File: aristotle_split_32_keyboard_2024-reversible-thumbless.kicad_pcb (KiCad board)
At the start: 2 copper layers, 100 x 87.7 mm, 41 parts, among them J1 8P8C, J2 Screw_Terminal_01x04, J3 Screw_Terminal_01x04, K13 SW_SPDT, K14 SW_SPDT, K15 SW_SPDT, K16 SW_SPDT, K17 SW_SPDT, K23 SW_SPDT, K24 SW_SPDT, K25 SW_SPDT, K26 SW_SPDT, K27 SW_SPDT, K4 SW_SPDT, K5 SW_SPDT, K6 SW_SPDT, K7 SW_SPDT, SW1 SW_SPDT, U1 ProMicro

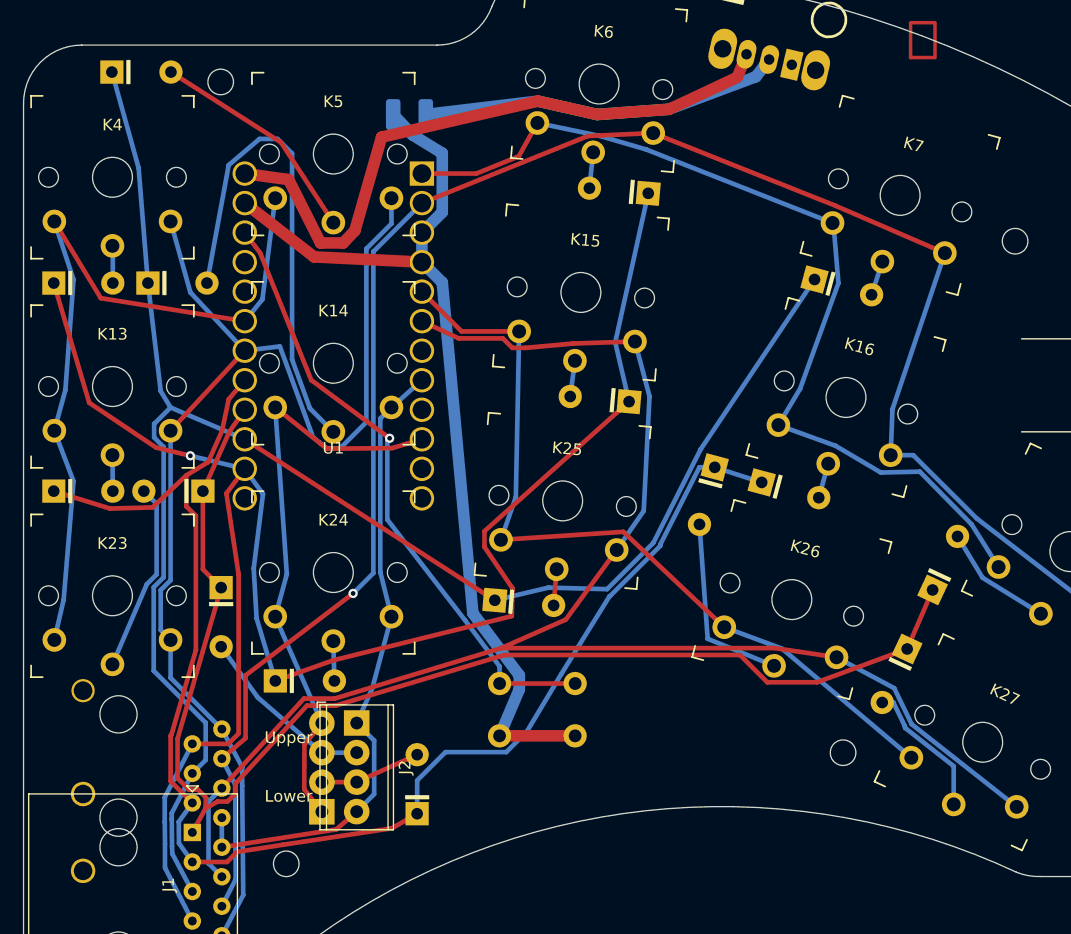
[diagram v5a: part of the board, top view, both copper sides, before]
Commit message: Reassign MCU pins to rows/columns
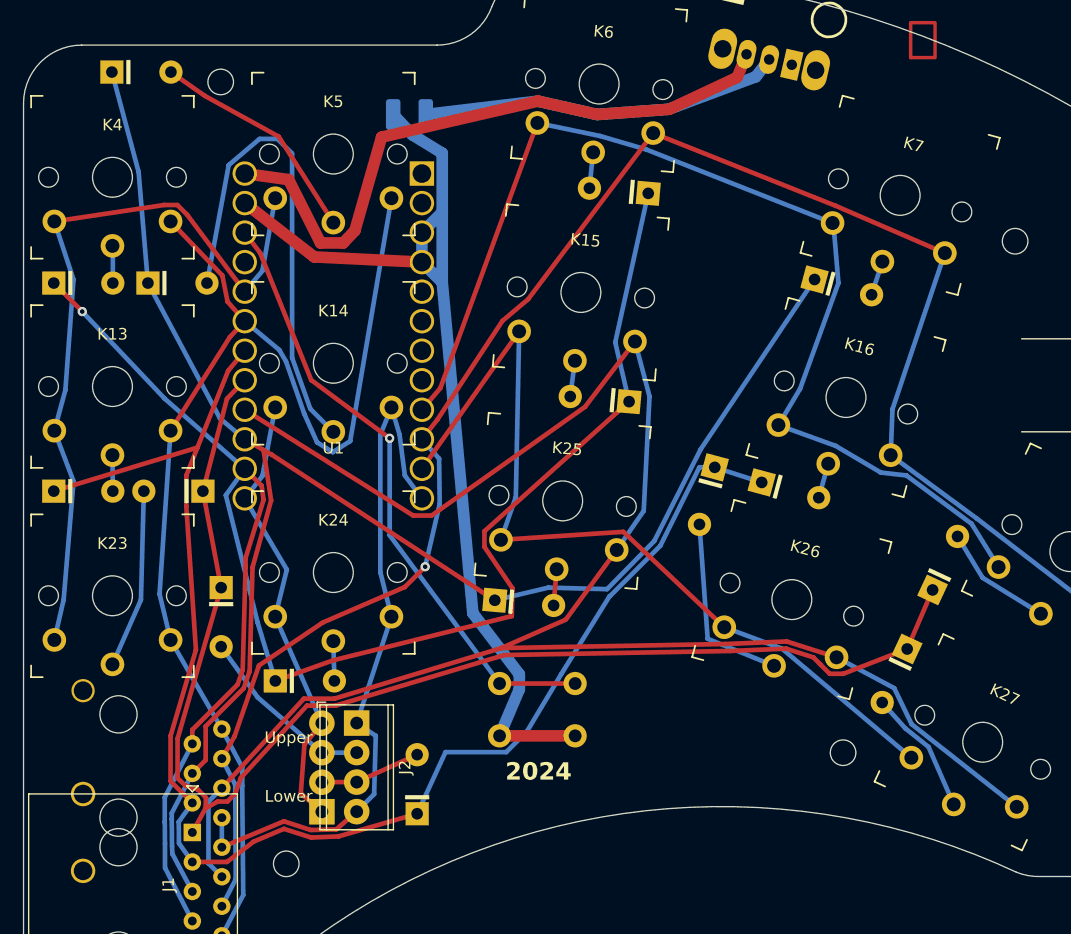
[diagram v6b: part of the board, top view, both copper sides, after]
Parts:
- U1: value ProMicro -> ProMicro_r
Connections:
- U1 pad 1: col6 -> unconnected-(U1-D3/TX-Pad1)
- U1 pad 10: col4 -> col1
- U1 pad 11: unconnected-(U1-B4-Pad11) -> col5
- U1 pad 12: unconnected-(U1-B5-Pad12) -> col3
- U1 pad 13: unconnected-(U1-B6-Pad13) -> col4
- U1 pad 16: row3 -> col2
- U1 pad 17: row2 -> row3
- U1 pad 18: col0 -> row2
- U1 pad 19: col7 -> col0
- U1 pad 2: col1 -> unconnected-(U1-D2/RX-Pad2)
- U1 pad 20: unconnected-(U1-F4-Pad20) -> col7
- U1 pad 5: col5 -> unconnected-(U1-D1/SDA-Pad5)
- U1 pad 6: col2 -> unconnected-(U1-D0/SCL-Pad6)
- U1 pad 8: col3 -> unconnected-(U1-C6-Pad8)
- U1 pad 9: unconnected-(U1-D7-Pad9) -> col6
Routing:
- net col2: track 137.4 -> 160.5 mm
- net col6: track 81.0 -> 95.4 mm
- net col4: track 50.8 -> 38.7 mm
- net row1: track 150.2 -> 143.1 mm
- net col1: track 158.7 -> 151.7 mm
- net GND: track 82.1 -> 88.2 mm
- net col3: track 55.4 -> 60.8 mm
- net col5: track 70.3 -> 75.0 mm
- net row0: track 152.9 -> 149.1 mm
- net col7: track 68.3 -> 65.7 mm
- net col0: track 106.8 -> 105.1 mm
- net row2: track 125.4 -> 127.0 mm
- net row3: track 112.5 -> 113.9 mm
- net Net-(D27-A): track 12.0 -> 10.9 mm
- net Net-(D23-A): track 16.3 -> 15.4 mm
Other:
- board text added: "2024"

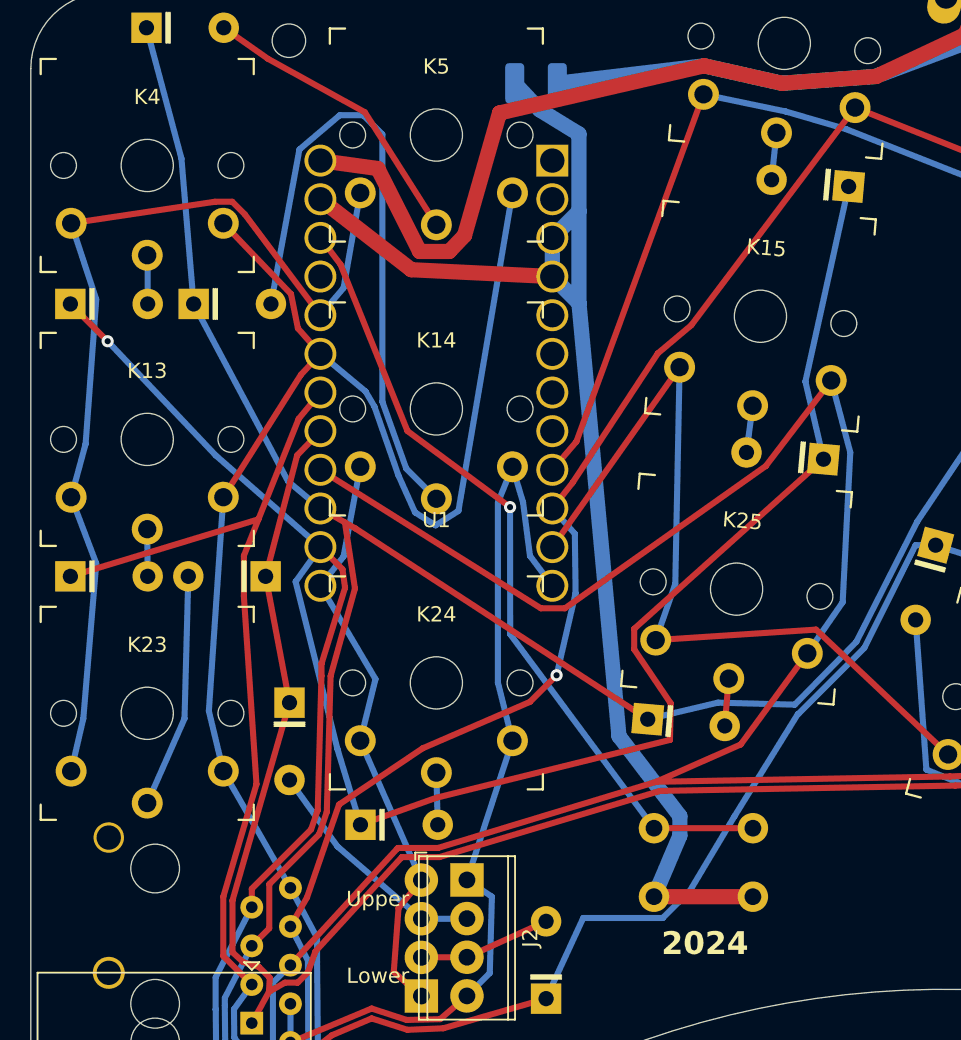
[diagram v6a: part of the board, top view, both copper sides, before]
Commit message: Move pins; update symbol library with pin numbers
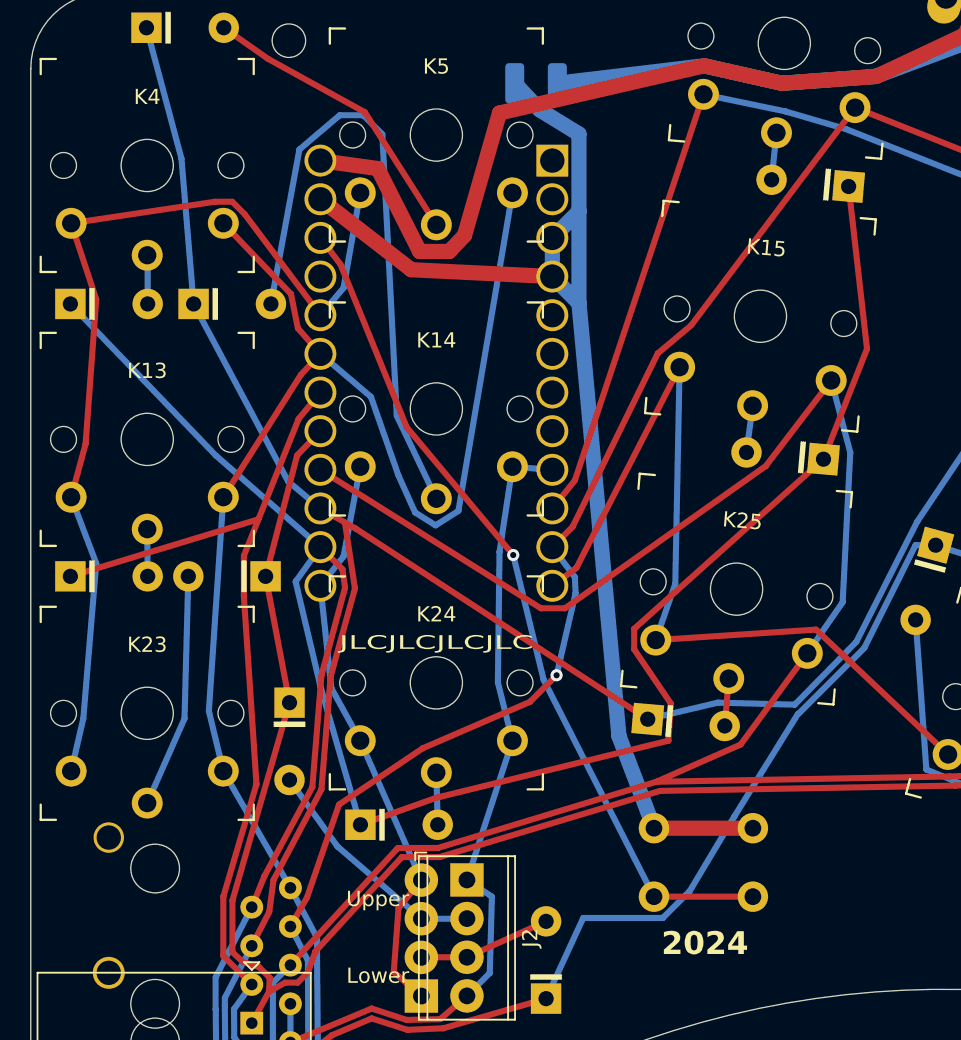
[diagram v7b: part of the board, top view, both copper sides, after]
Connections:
- RESET1 pad 1: Net-(U1-RST) -> GND
- RESET1 pad 2: GND -> Net-(U1-RST)
- U1 pad 10: col1 -> col6
- U1 pad 11: col5 -> col1
- U1 pad 12: col3 -> col5
- U1 pad 9: col6 -> col3
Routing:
- net col3: track 60.8 -> 54.8 mm
- net GND: track 88.2 -> 82.4 mm
- net Net-(U1-RST): track 53.1 -> 55.6 mm
- net col6: track 95.4 -> 97.7 mm
- net col5: track 75.0 -> 77.3 mm
- net row1: track 143.1 -> 142.3 mm
- net row0: track 149.1 -> 148.4 mm, vias 1 -> 0
- net col4: track 38.7 -> 38.1 mm

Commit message: Final production version
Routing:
- net row1: track 142.3 -> 141.7 mm
